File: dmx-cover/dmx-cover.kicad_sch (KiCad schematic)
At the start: 7 parts

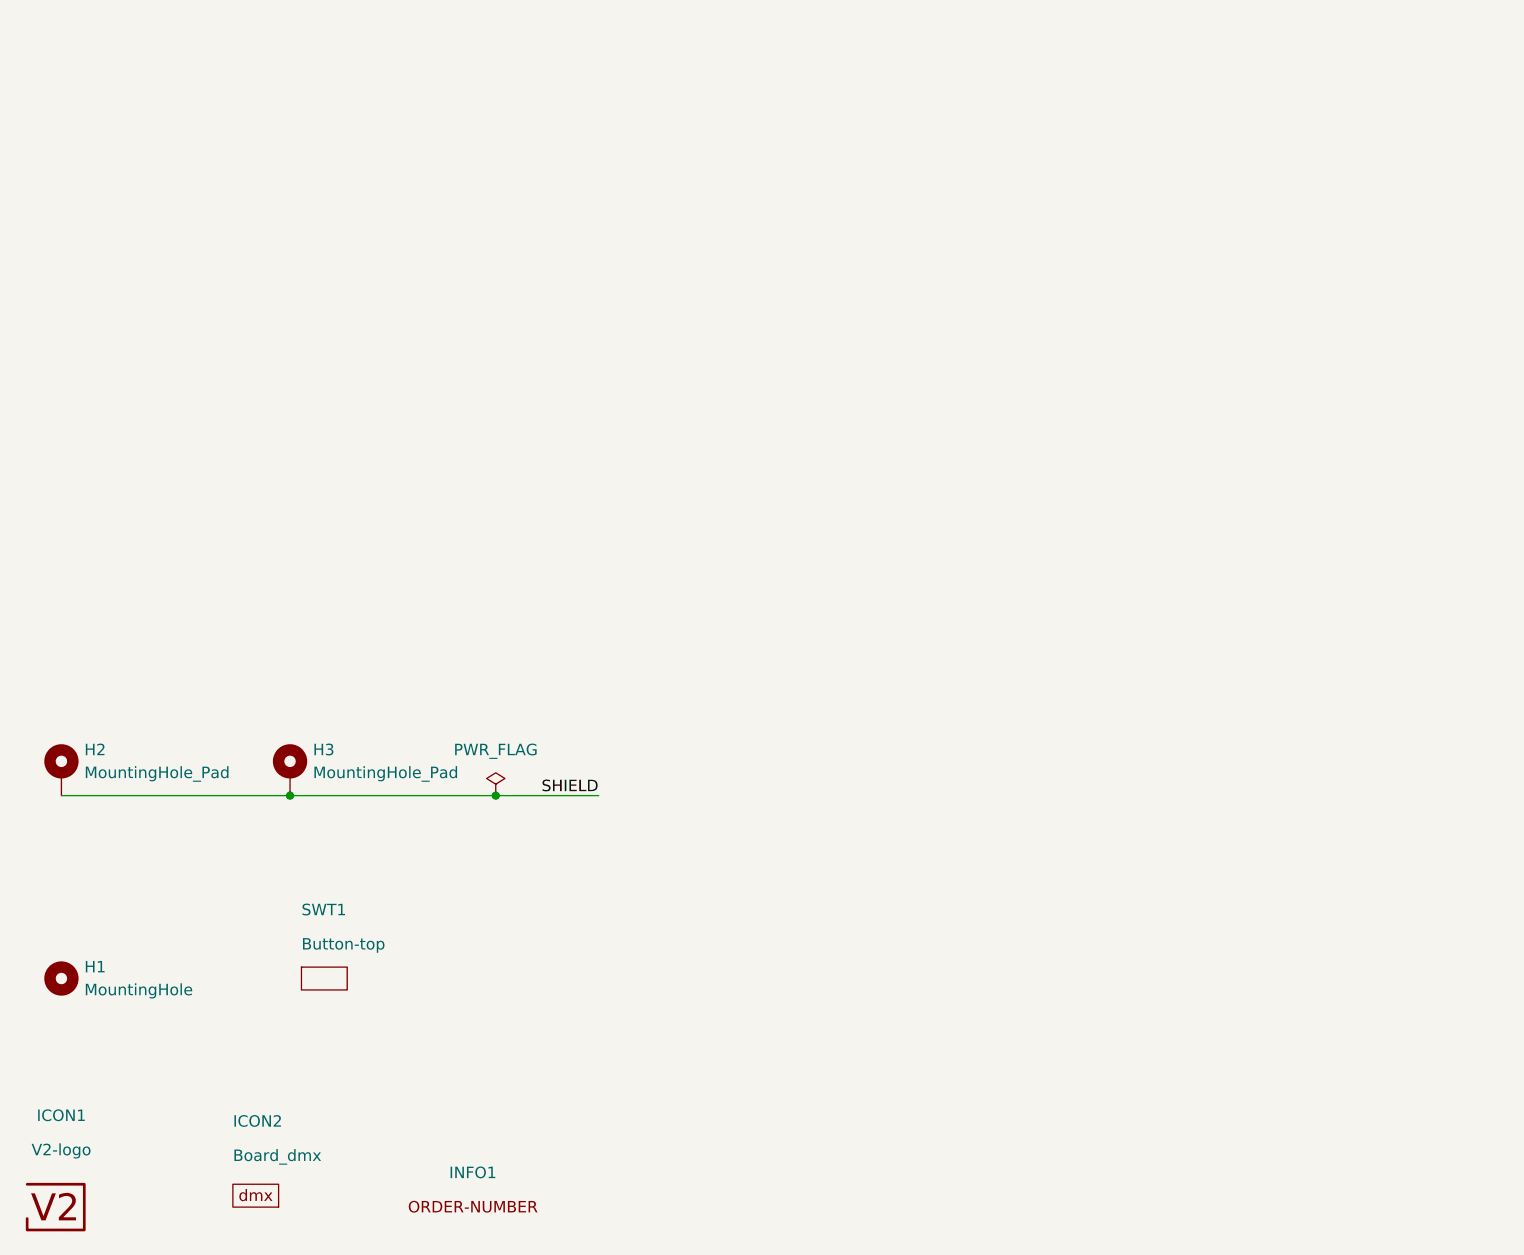
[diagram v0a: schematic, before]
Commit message: Update to KiCad 7.0
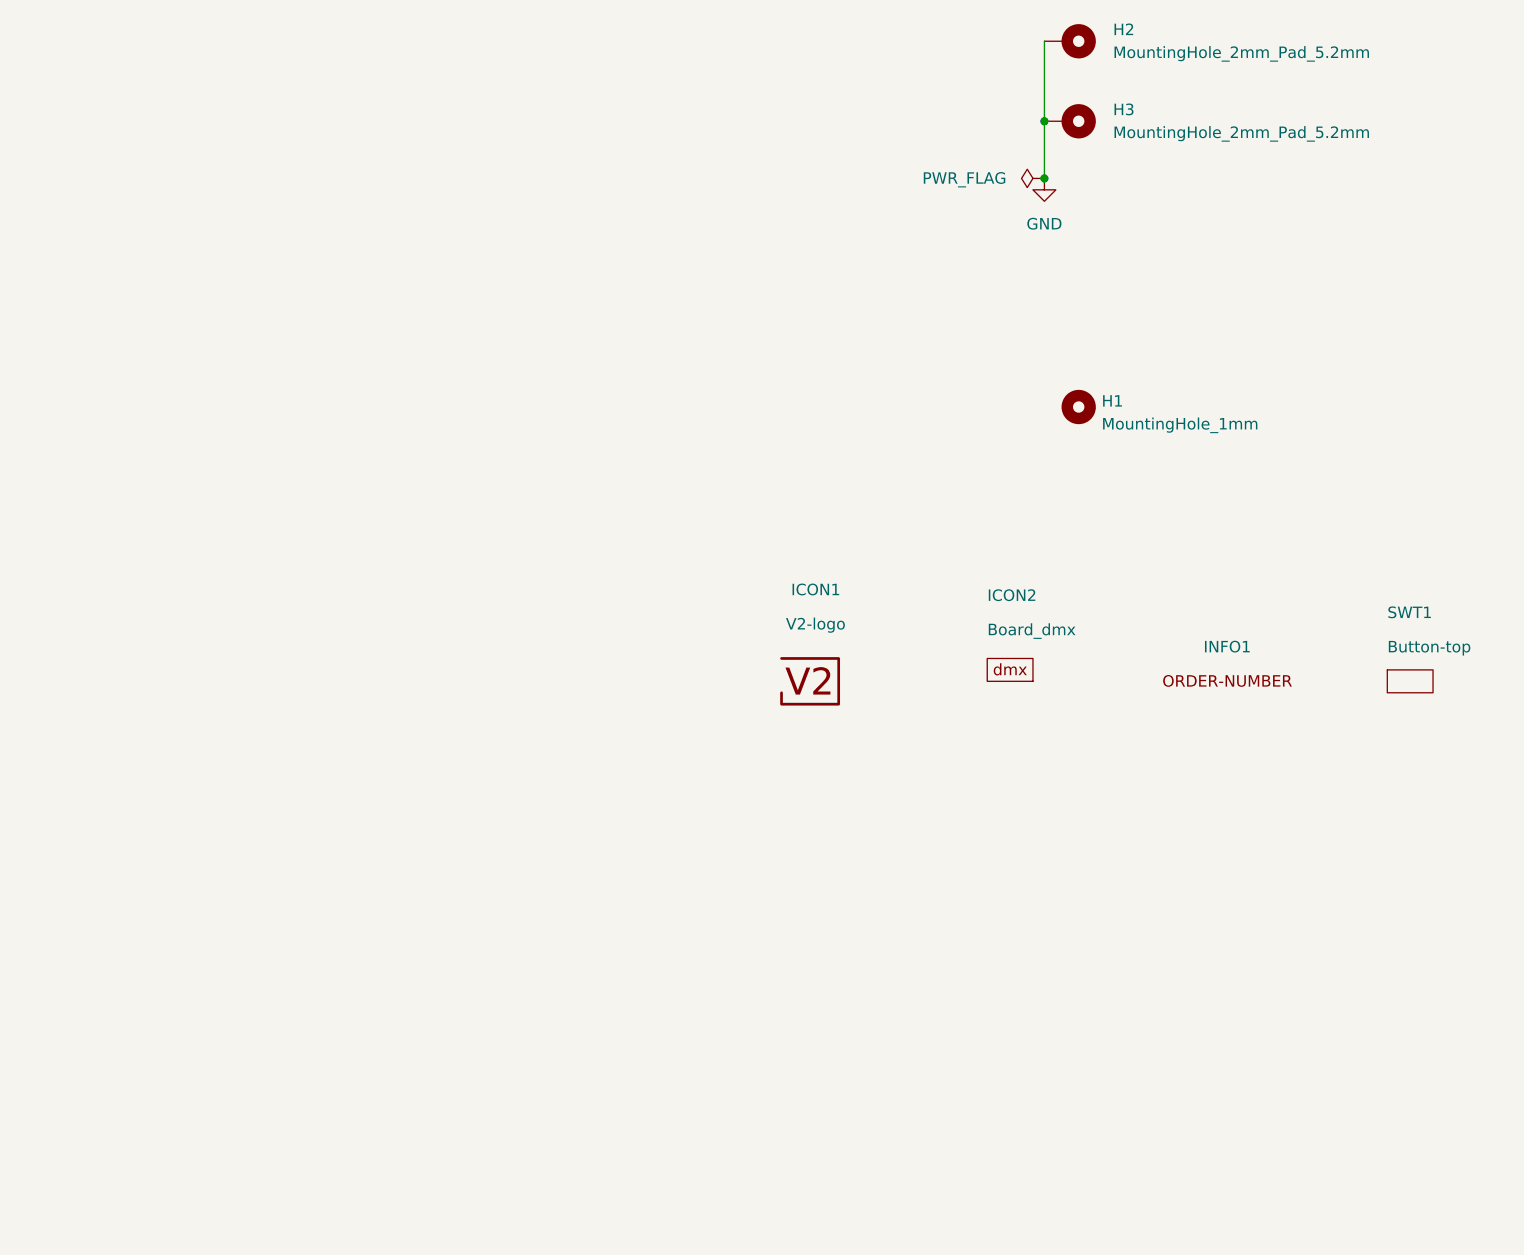
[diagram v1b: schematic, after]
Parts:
- H1: value MountingHole -> MountingHole_1mm; footprint V2_Mechanical:Mounting_Hole_1 -> V2_Mechanical:MountingHole_1mm; symbol Mechanical:MountingHole -> V2_Mechanical:MountingHole_1mm
- H2, H3: value MountingHole_Pad -> MountingHole_2mm_Pad_5.2mm; footprint V2_Mechanical:Mounting_Hole_Pad_2-5.2 -> V2_Mechanical:Mounting_Hole_2mm_Pad_5.2mm; symbol Mechanical:MountingHole_Pad -> V2_Mechanical:MountingHole_2mm_Pad_5.2mm
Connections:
- net SHIELD renamed GND
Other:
- company: (none) -> Versio Dup
- title: (none) -> V2 dmx
- moved on the sheet: H1, H2, H3, ICON1, ICON2, INFO1, SWT1
